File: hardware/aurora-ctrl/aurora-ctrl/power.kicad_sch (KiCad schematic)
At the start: 0 parts

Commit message: M2: TPS5430 12V->5V buck stage wired and annotated, ERC clean
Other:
- added sheet 12V_Buck1 (power_12v_sch.kicad_sch)
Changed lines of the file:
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@@
 	(generator_version "10.0")
 	(paper "A4")
+	(sheet
+		(at 17.78 186.69)
+		(size 12.7 3.81)
+		(exclude_from_sim no)
+		(in_bom yes)
+		(on_board yes)
+		(dnp no)
+		(fields_autoplaced yes)
+		(stroke
+			(width 0.1524)
+			(type solid)
+		)
+		(fill
+			(color 0 0 0 0)
+		)
+		(property "Sheetname" "12V_Buck1"
+			(at 17.78 185.9784 0)
+			(show_name no)
+			(do_not_autoplace no)
+			(effects
+				(font
+					(size 1.27 1.27)
+				)
+				(justify left bottom)
+			)
+		)
+		(property "Sheetfile" "power_12v_sch.kicad_sch"
+			(at 17.78 191.0846 0)
+			(show_name no)
+			(do_not_autoplace no)
+			(effects
+				(font
+					(size 1.27 1.27)
+				)
+				(justify left top)
+			)
+		)
+		(instances
+			(project "aurora-ctrl"
+				(path "/be3cfc26-2ede-416c-b0d2-d4a4334eaee3/4092f569-4a59-4d42-aaa9-629788cd0217"
+					(page "9")
+				)
+			)
+		)
+	)
 )

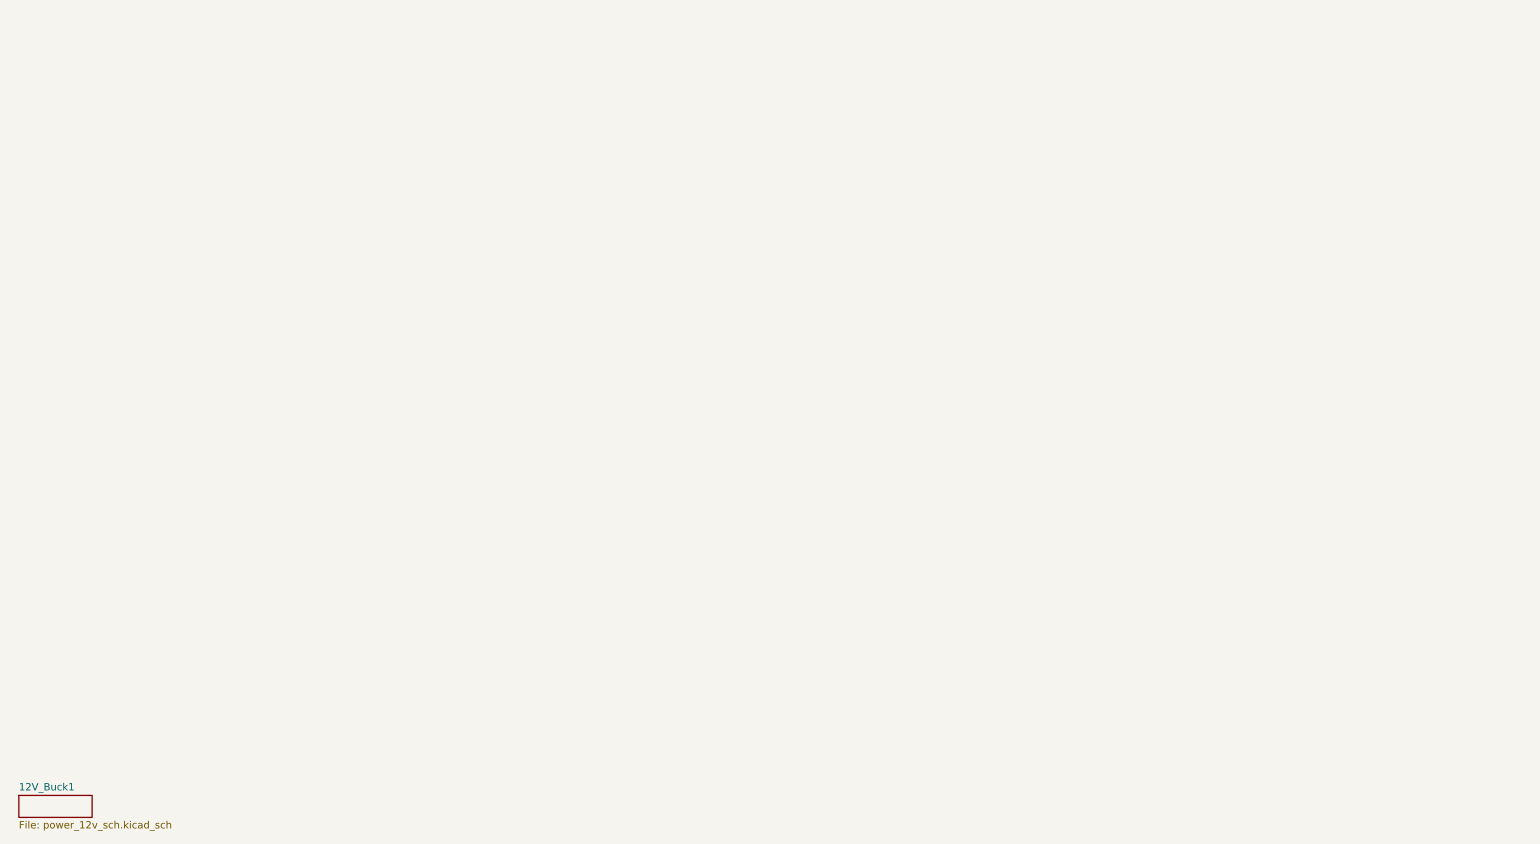
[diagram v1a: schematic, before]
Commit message: M3 complete: MSPM0G3507 MCU sheet wired - power, SWD, CAN, I2C, SPI, UART, ADC reserved
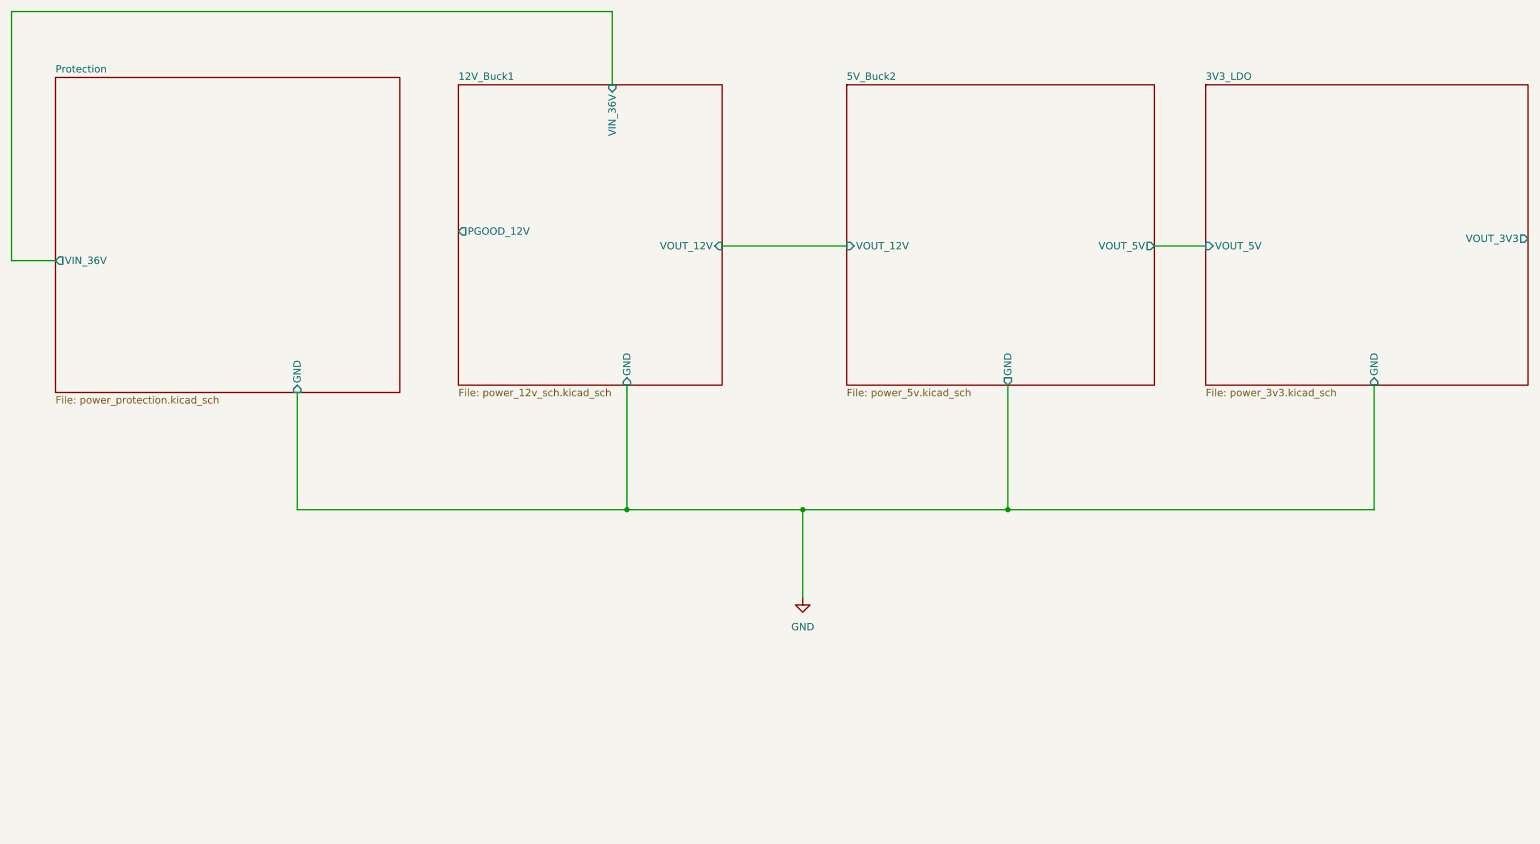
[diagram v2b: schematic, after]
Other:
- added sheet 3V3_LDO (power_3v3.kicad_sch)
- added sheet 5V_Buck2 (power_5v.kicad_sch)
- added sheet Protection (power_protection.kicad_sch)
- sheet 12V_Buck1 ports: added GND, PGOOD_12V, VIN_36V, VOUT_12V; removed none
